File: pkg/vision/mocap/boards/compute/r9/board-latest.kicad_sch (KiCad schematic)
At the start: 13 parts, among them J10 AUX, J4 Conn_01x08, Q2 BSS138

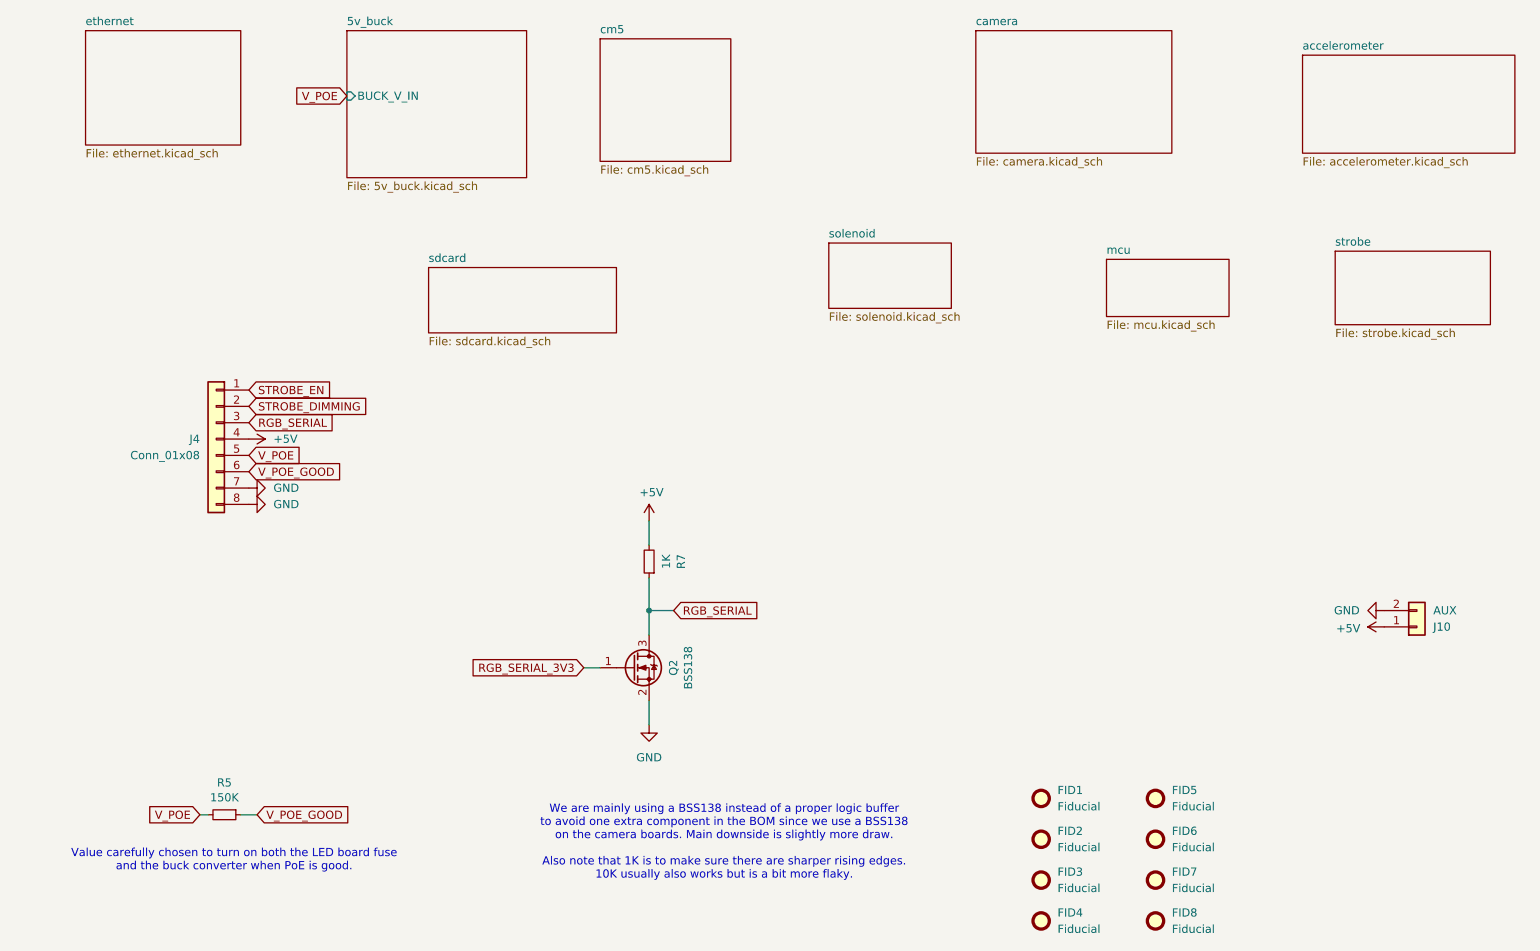
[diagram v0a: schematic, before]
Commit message: New mocap compute board revisions.
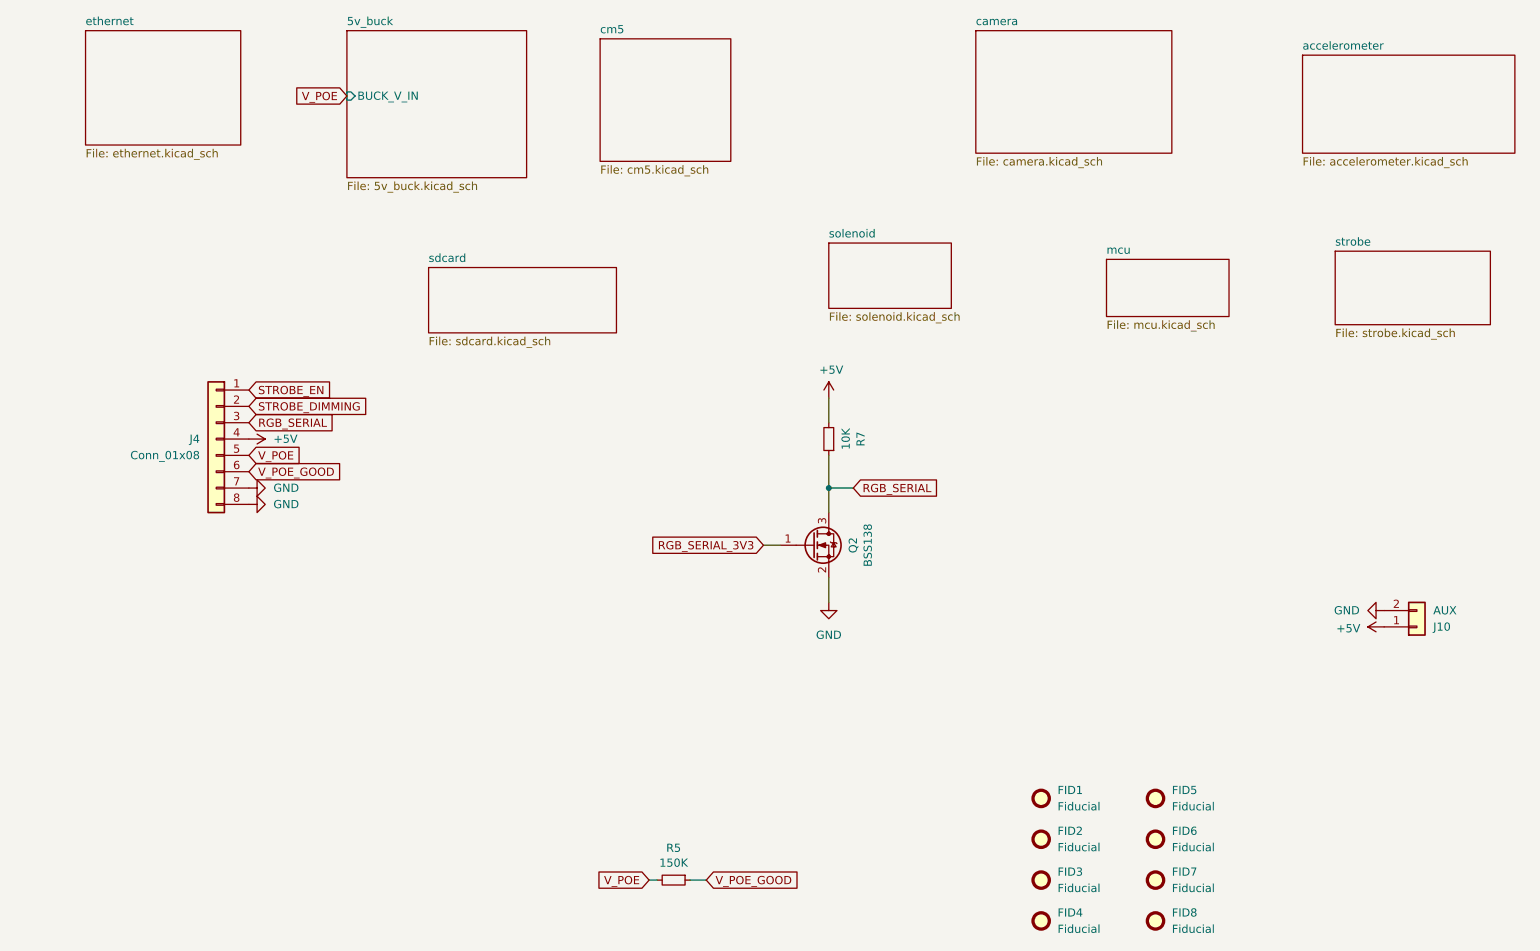
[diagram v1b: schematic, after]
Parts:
- R7: value 1K -> 10K
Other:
- note removed: "Value carefully chosen to turn on both the LED board fuse and the buck converter when PoE is good."
- note removed: "We are mainly using a BSS138 instead of a proper logic buffer to avoid one extra component in the BOM since we use a BSS138 on the camera boards. Main downside is slightly more draw. Also note that 1K is to make sure there are sharper rising edges. 10K usually also works but is a bit more flaky."
- moved on the sheet: Q2, R5, R7
